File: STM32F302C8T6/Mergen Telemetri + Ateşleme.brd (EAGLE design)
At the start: 49.7 x 87.5 mm, 91 parts, among them J2 U.FL, Q2 IRLML6344TRPBF, Q3 IRLML6344TRPBF, U2 BMP280, U3 MPU-6050, U4 L86, U6 AMS1117-3.3, U7 AMS1117-3.3, U8 STM32F302C8T6, X1 JST-XH-04-PIN-LONG-PAD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

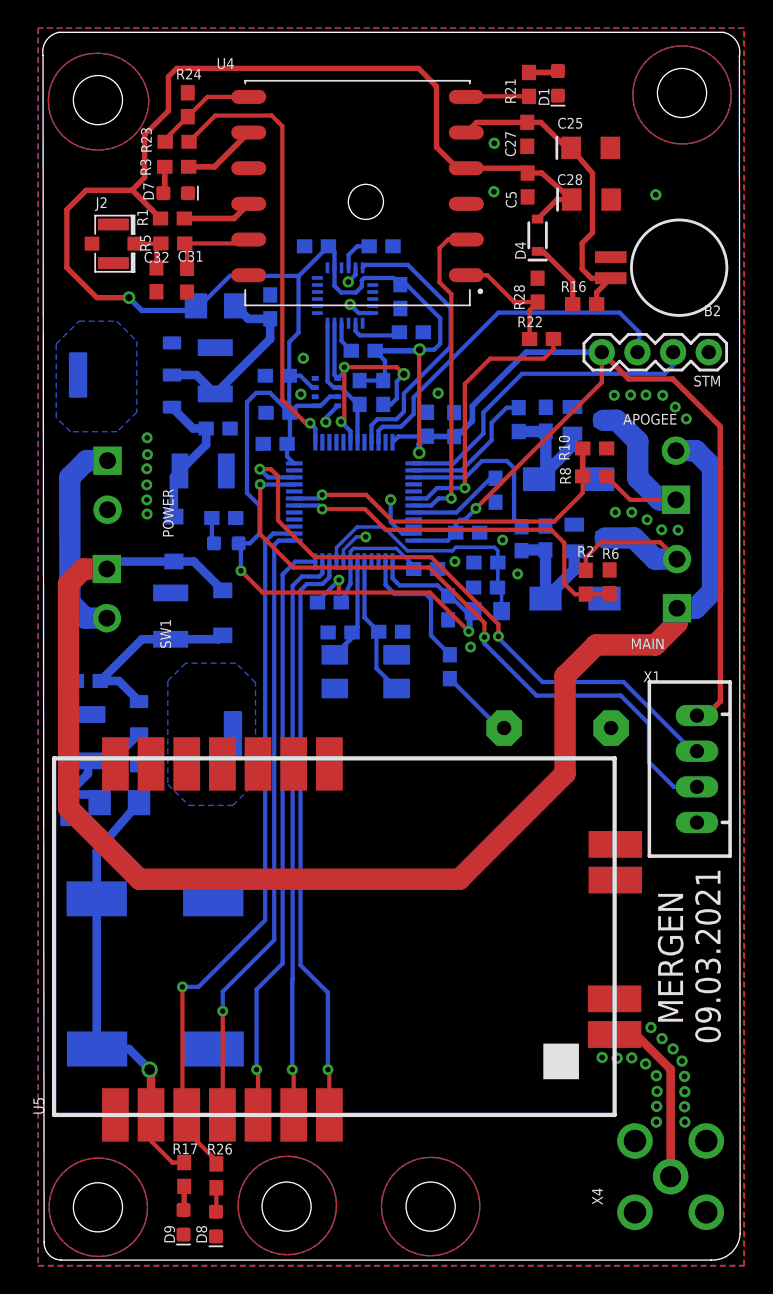
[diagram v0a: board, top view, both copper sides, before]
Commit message: 5V lineer regülator was added for ignition outputs
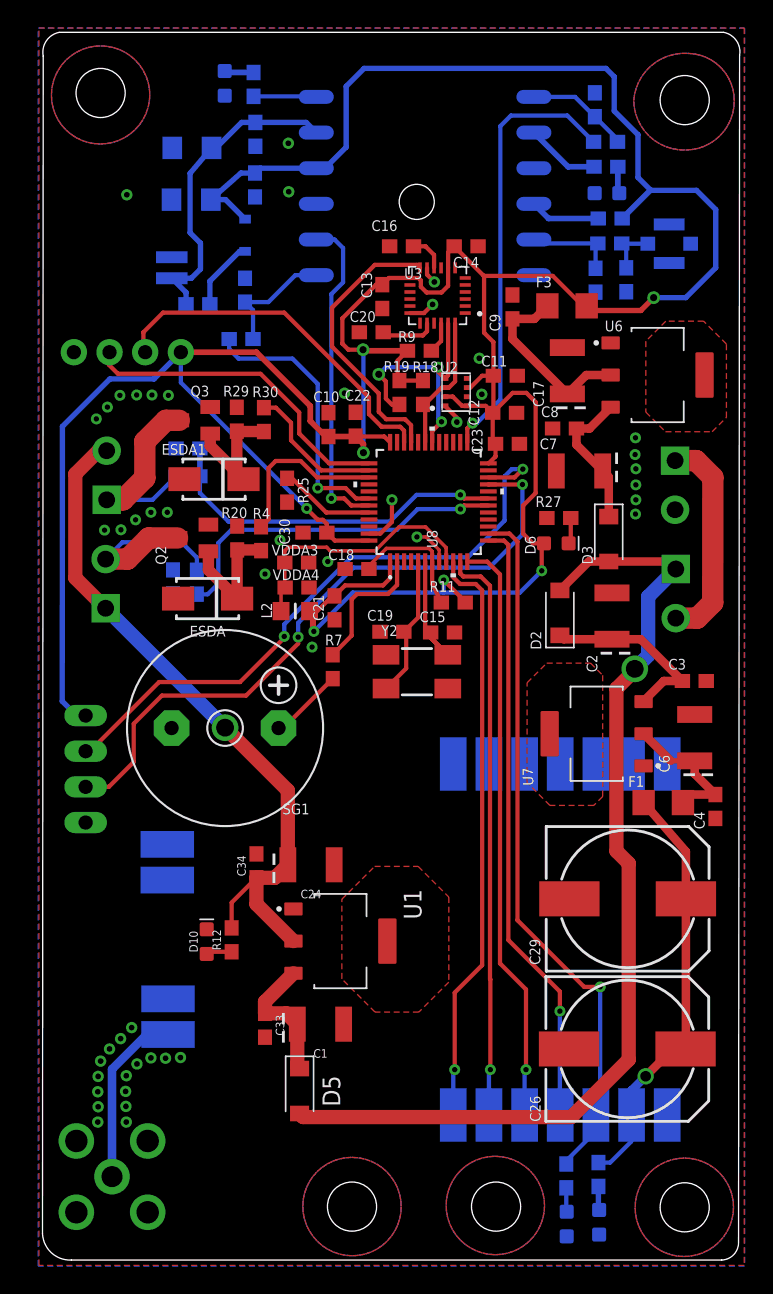
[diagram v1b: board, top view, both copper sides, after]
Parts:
- added C1, C24: 22uF, SparkFun-Capacitors:EIA3528
- added C33, C34: 100nF, SparkFun-Capacitors:0603
- added D10: (no value), SparkFun-LED:LED-0603
- added D5: B5819W, Diode:SODFL3718X115
- added R12: 1k5, SparkFun-Resistors:0603
- added U1: AMS1117-3.3, AMS1117-3.3:SOT229P700X180-4N
- moved C4 46.2 mm to (48.7, 32.9), flipped to the top
- moved STM 45.2 mm to (3.02, 65.2), flipped to the bottom
- moved X1 43.5 mm to (3.86, 35.5), flipped to the bottom
- moved C6 43.2 mm to (47.2, 37.8), flipped to the top
- moved C3 43.2 mm to (47.2, 41.8), flipped to the top
- moved B2 41.0 mm to (5.13, 71.3), flipped to the bottom
- moved MAIN 40.7 mm to (5.28, 47.0), flipped to the bottom
- moved APOGEE 40.6 mm to (5.36, 54.7), flipped to the bottom
- moved SW1 40.5 mm to (45.9, 49.8), flipped to the bottom
- moved POWER 40.4 mm to (45.8, 57.5), flipped to the bottom
- moved X4 39.8 mm to (5.74, 6.52), flipped to the bottom
- moved J2 39.6 mm to (45.4, 73.0), flipped to the bottom
- moved F1 38.7 mm to (45.0, 33.2), flipped to the top
- moved U6 37.9 mm to (44.6, 63.6), flipped to the top
- moved C29 33.7 mm to (42.5, 26.3), flipped to the top
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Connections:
- new net HT3: U1.4
- new net N$23: C1.A, C33.1, D5.1, U1.3
- new net N$25: D10.A, R12.1
- new net VOUT: APOGEE.2, C24.A, C34.1, MAIN.1, R12.2, U1.2
- net GND: now also C1.C, C24.C, C33.2, C34.2, D10.C, U1.1
- net VCC: now also D5.2; no longer APOGEE.2, MAIN.1
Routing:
- net VOUT: track 0.00 -> 49.6 mm, vias 0 -> 1
- net VCC: track 101.6 -> 71.6 mm, vias 0 -> 1
- net N$23: track 0.00 -> 9.54 mm
- net N$25: track 0.00 -> 1.84 mm
- net 5V: track 31.2 -> 30.4 mm
- added copper zone on layer 1, net HT
- added copper zone on layer 1, net HT2
- added copper zone on layer 1, net HT3
- removed copper zone on layer 16, net HT
- removed copper zone on layer 16, net HT2
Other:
- outline, holes or cut-outs redrawn
